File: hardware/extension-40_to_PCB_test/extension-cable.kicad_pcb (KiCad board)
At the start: 2 copper layers, 74 x 43 mm, 55 parts, among them J1 XKTF-005, J2 Conn_01x08_Socket, U1 ED078KH6

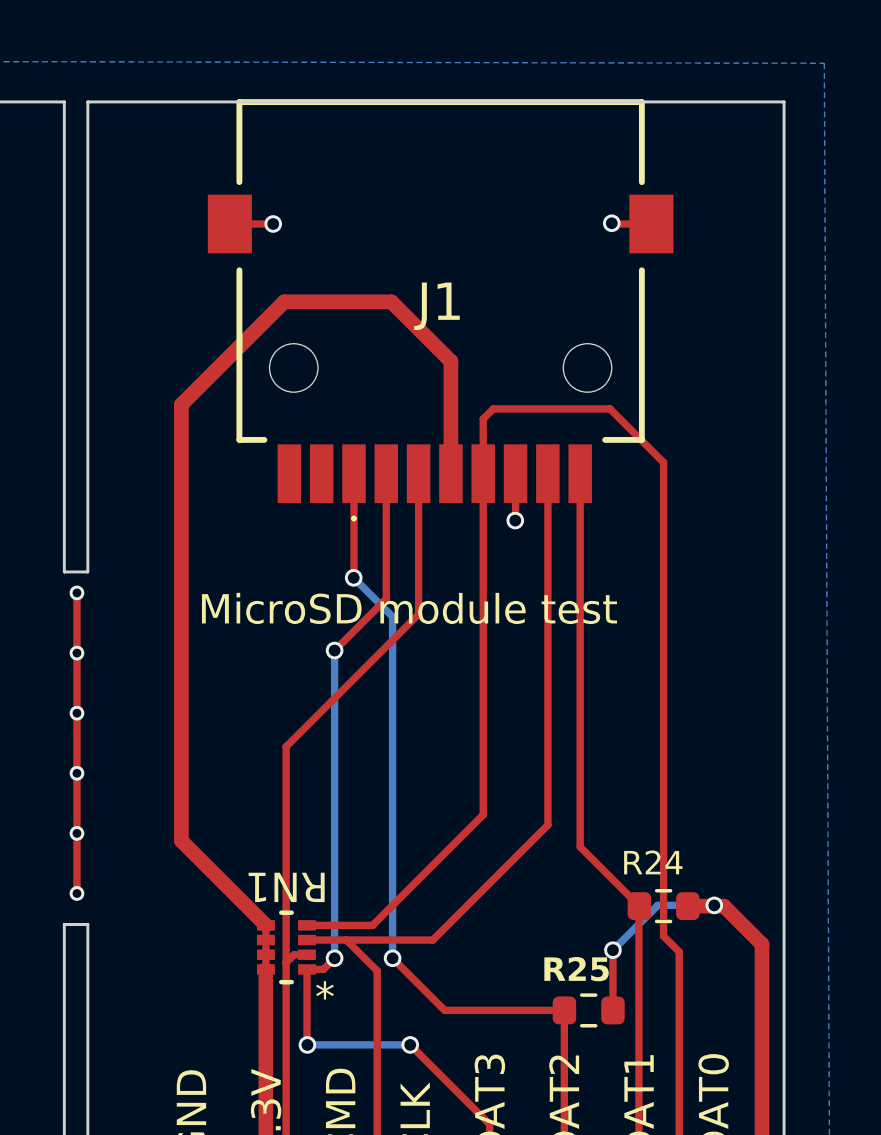
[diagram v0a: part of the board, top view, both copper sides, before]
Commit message: 40 pin FPC tester sent to fabrication
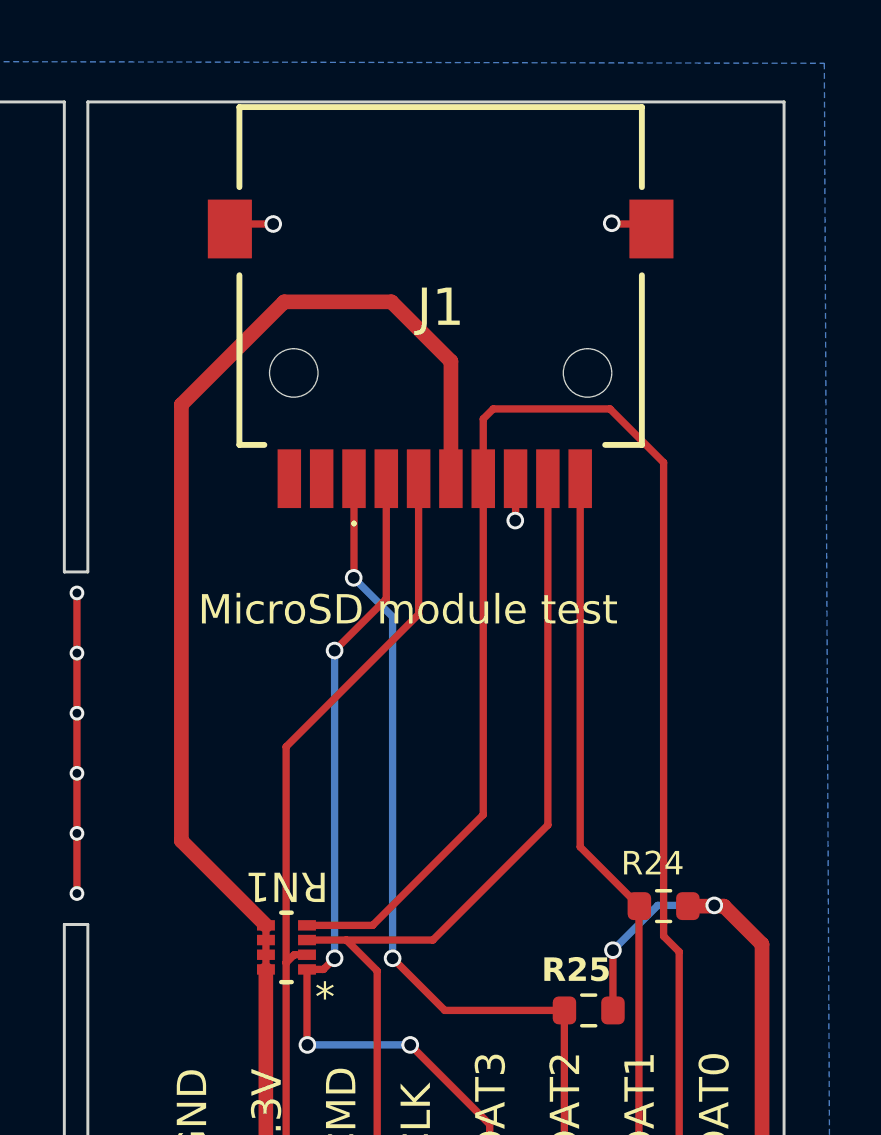
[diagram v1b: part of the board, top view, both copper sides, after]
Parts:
- CKV1, EP_MODE1, LEH1, OE1, STV1, XCL1, XSTL1: value LED GREEN -> LED RED
- moved J1 0.17 mm to (132.3, 65.0)
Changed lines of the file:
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@@
       (plot_on_all_layers_selection 0x0000000_00000000)
       (disableapertmacros false)
-      (usegerberextensions false)
+      (usegerberextensions true)
       (usegerberattributes true)
       (usegerberadvancedattributes false)
@@
       (plotinvisibletext false)
       (sketchpadsonfab false)
-      (subtractmaskfromsilk false)
+      (subtractmaskfromsilk true)
       (outputformat 1)
       (mirror false)
@@
     (descr "LED SMD 0805 (2012 Metric), square (rectangular) end terminal, IPC_7351 nominal, (Body size source: https://docs.google.com/spreadsheets/d/1BsfQQcO9C6DZCsRaXUlFlo91Tg2WpOkGARC1WS5S8t0/edit?usp=sharing), generated with kicad-footprint-generator")
     (tags "LED")
-    (property "LCSC" "C2297")
+    (property "LCSC" "C84256")
     (property "Sheetfile" "extension-cable.kicad_sch")
     (property "Sheetname" "")
@@
         (effects (font (size 0.8 0.8) (thickness 0.15)))
     )
-    (fp_text value "LED GREEN" (at 0 1.65) (layer "F.Fab") hide
+    (fp_text value "LED RED" (at 0 1.65) (layer "F.Fab") hide
         (effects (font (size 1 1) (thickness 0.15)))
     )
@@
     (descr "LED SMD 0805 (2012 Metric), square (rectangular) end terminal, IPC_7351 nominal, (Body size source: https://docs.google.com/spreadsheets/d/1BsfQQcO9C6DZCsRaXUlFlo91Tg2WpOkGARC1WS5S8t0/edit?usp=sharing), generated with kicad-footprint-generator")
     (tags "LED")
-    (property "LCSC" "C2297")
+    (property "LCSC" "C84256")
     (property "Sheetfile" "extension-cable.kicad_sch")
     (property "Sheetname" "")
@@
         (effects (font (size 1 1) (thickness 0.15)))
     )
-    (fp_text value "LED GREEN" (at 0 1.65) (layer "F.Fab") hide
+    (fp_text value "LED RED" (at 0 1.65) (layer "F.Fab") hide
         (effects (font (size 1 1) (thickness 0.15)))
     )
@@
     (property "ki_description" "test point")
     (property "ki_keywords" "test point tp")
-    (attr exclude_from_pos_files)
+    (attr exclude_from_pos_files exclude_from_bom)
     (fp_text reference "TP1" (at 0 -1.998) (layer "F.SilkS")
         (effects (font (size 0.8 0.8) (thickness 0.15)))
@@
     (descr "LED SMD 0805 (2012 Metric), square (rectangular) end terminal, IPC_7351 nominal, (Body size source: https://docs.google.com/spreadsheets/d/1BsfQQcO9C6DZCsRaXUlFlo91Tg2WpOkGARC1WS5S8t0/edit?usp=sharing), generated with kicad-footprint-generator")
     (tags "LED")
-    (property "LCSC" "C2297")
+    (property "LCSC" "C84256")
     (property "Sheetfile" "extension-cable.kicad_sch")
     (property "Sheetname" "")
@@
         (effects (font (size 1 1) (thickness 0.15)))
     )
-    (fp_text value "LED GREEN" (at 0 1.65) (layer "F.Fab") hide
+    (fp_text value "LED RED" (at 0 1.65) (layer "F.Fab") hide
         (effects (font (size 1 1) (thickness 0.15)))
     )
@@
     (descr "LED SMD 0805 (2012 Metric), square (rectangular) end terminal, IPC_7351 nominal, (Body size source: https://docs.google.com/spreadsheets/d/1BsfQQcO9C6DZCsRaXUlFlo91Tg2WpOkGARC1WS5S8t0/edit?usp=sharing), generated with kicad-footprint-generator")
     (tags "LED")
-    (property "LCSC" "C2297")
+    (property "LCSC" "C84256")
     (property "Sheetfile" "extension-cable.kicad_sch")
     (property "Sheetname" "")
@@
         (effects (font (size 1 1) (thickness 0.15)))
     )
-    (fp_text value "LED GREEN" (at 0 1.65) (layer "F.Fab")
+    (fp_text value "LED RED" (at 0 1.65) (layer "F.Fab")
         (effects (font (size 1 1) (thickness 0.15)))
     )
@@
   )
   (footprint "SD:XKTF005-SD" (layer "F.Cu")
-    (at 132.31 64.83 180)
+    (at 132.31 65 180)
     (descr "XKTF-005-1")
     (tags "Connector")
@@
     (descr "LED SMD 0805 (2012 Metric), square (rectangular) end terminal, IPC_7351 nominal, (Body size source: https://docs.google.com/spreadsheets/d/1BsfQQcO9C6DZCsRaXUlFlo91Tg2WpOkGARC1WS5S8t0/edit?usp=sharing), generated with kicad-footprint-generator")
     (tags "LED")
-    (property "LCSC" "C2297")
+    (property "LCSC" "C84256")
     (property "Sheetfile" "extension-cable.kicad_sch")
     (property "Sheetname" "")
@@
         (effects (font (size 0.8 0.8) (thickness 0.14) bold))
     )
-    (fp_text value "LED GREEN" (at 0 1.65) (layer "F.Fab") hide
+    (fp_text value "LED RED" (at 0 1.65) (layer "F.Fab") hide
         (effects (font (size 1 1) (thickness 0.15)))
     )
@@
     (descr "LED SMD 0805 (2012 Metric), square (rectangular) end terminal, IPC_7351 nominal, (Body size source: https://docs.google.com/spreadsheets/d/1BsfQQcO9C6DZCsRaXUlFlo91Tg2WpOkGARC1WS5S8t0/edit?usp=sharing), generated with kicad-footprint-generator")
     (tags "LED")
-    (property "LCSC" "C2297")
+    (property "LCSC" "C84256")
     (property "Sheetfile" "extension-cable.kicad_sch")
     (property "Sheetname" "")
@@
         (effects (font (size 1 1) (thickness 0.15)))
     )
-    (fp_text value "LED GREEN" (at 0 1.65) (layer "F.Fab")
+    (fp_text value "LED RED" (at 0 1.65) (layer "F.Fab")
         (effects (font (size 1 1) (thickness 0.15)))
     )
@@
     (pad "41" smd rect (at -11.65 0.575) (size 1.8 2.2) (layers "F.Cu" "F.Paste" "F.Mask"))
     (pad "42" smd rect (at 11.65 0.575) (size 1.8 2.2) (layers "F.Cu" "F.Paste" "F.Mask"))
-    (model "${KIPRJMOD}/3dmodels/FH12-40S-0.5SH_55.step"
+    (model "${KIPRJMOD}/../epdiy-v7/3dmodels/FH12-40S-0.5SH_55.step"
       (offset (xyz 0 -0.2199999955 0.999999985))
       (scale (xyz 1 1 1))
@@
     (descr "LED SMD 0805 (2012 Metric), square (rectangular) end terminal, IPC_7351 nominal, (Body size source: https://docs.google.com/spreadsheets/d/1BsfQQcO9C6DZCsRaXUlFlo91Tg2WpOkGARC1WS5S8t0/edit?usp=sharing), generated with kicad-footprint-generator")
     (tags "LED")
-    (property "LCSC" "C2297")
+    (property "LCSC" "C84256")
     (property "Sheetfile" "extension-cable.kicad_sch")
     (property "Sheetname" "")
@@
         (effects (font (size 1 1) (thickness 0.15)))
     )
-    (fp_text value "LED GREEN" (at 0 1.65) (layer "F.Fab") hide
+    (fp_text value "LED RED" (at 0 1.65) (layer "F.Fab") hide
         (effects (font (size 1 1) (thickness 0.15)))
     )
@@
     (property "ki_description" "Generic connector, single row, 01x08, script generated")
     (property "ki_keywords" "connector")
-    (attr through_hole)
+    (attr through_hole exclude_from_pos_files exclude_from_bom)
     (fp_text reference "J2" (at -2.87 -0.345 180) (layer "F.SilkS") hide
         (effects (font (size 1 1) (thickness 0.15)))
@@
   (segment (start 127.76 90.085) (end 127.76 87.53) (width 0.25) (layer "F.Cu") (net 64))
   (segment (start 133.98 93.855) (end 133.98 92.805) (width 0.25) (layer "F.Cu") (net 64))
-  (segment (start 128.7 76.675) (end 130.46 74.915) (width 0.25) (layer "F.Cu") (net 64))
   (segment (start 127.76 87.53) (end 128.32 87.53) (width 0.25) (layer "F.Cu") (net 64))
+  (segment (start 128.7 76.675) (end 130.46 74.915) (width 0.25) (layer "F.Cu") (net 64))
   (segment (start 133.98 92.805) (end 131.275 90.1) (width 0.25) (layer "F.Cu") (net 64))
   (segment (start 133.98 95.955) (end 133.98 93.855) (width 0.25) (layer "F.Cu") (net 64))
@@
   (segment (start 128.7 87.15) (end 128.7 76.675) (width 0.25) (layer "B.Cu") (net 64))
   (segment (start 131.275 90.1) (end 127.775 90.1) (width 0.25) (layer "B.Cu") (net 64))
-  (segment (start 127.324978 87.029874) (end 127.76 87.029874) (width 0.25) (layer "F.Cu") (net 65))
   (segment (start 127.05 87.304852) (end 127.05 79.95) (width 0.25) (layer "F.Cu") (net 65))
   (segment (start 127.05 87.304852) (end 127.324978 87.029874) (width 0.25) (layer "F.Cu") (net 65))
   (segment (start 128.9 95.955) (end 127.05 94.105) (width 0.25) (layer "F.Cu") (net 65))
+  (segment (start 127.76 87.029874) (end 127.324978 87.029874) (width 0.25) (layer "F.Cu") (net 65))
   (segment (start 131.56 75.44) (end 131.56 70.655) (width 0.25) (layer "F.Cu") (net 65))
   (segment (start 127.05 79.95) (end 131.56 75.44) (width 0.25) (layer "F.Cu") (net 65))
@@
   (segment (start 138.075 68.45) (end 134.1 68.45) (width 0.25) (layer "F.Cu") (net 67))
   (segment (start 141.6 96.575) (end 139.9 98.275) (width 0.25) (layer "F.Cu") (net 68))
-  (segment (start 127.76 86.529748) (end 129.1 86.529748) (width 0.25) (layer "F.Cu") (net 68))
   (segment (start 141.6 95.955) (end 141.6 96.575) (width 0.25) (layer "F.Cu") (net 68))
   (segment (start 130.15 87.579748) (end 129.1 86.529748) (width 0.25) (layer "F.Cu") (net 68))
   (segment (start 129.1 86.529748) (end 132.045252 86.529748) (width 0.25) (layer "F.Cu") (net 68))
   (segment (start 139.9 98.275) (end 131.5 98.275) (width 0.25) (layer "F.Cu") (net 68))
+  (segment (start 127.76 86.529748) (end 129.1 86.529748) (width 0.25) (layer "F.Cu") (net 68))
   (segment (start 135.96 82.615) (end 135.96 70.655) (width 0.25) (layer "F.Cu") (net 68))
   (segment (start 132.045252 86.529748) (end 135.96 82.615) (width 0.25) (layer "F.Cu") (net 68))
